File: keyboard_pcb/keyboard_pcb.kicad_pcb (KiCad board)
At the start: 2 copper layers, 190 parts, among them SW1 ESC, SW10 F9, SW11 F10, SW12 F11, SW13 F12, SW14 PRNTSC, SW15 SCRLLK, SW16 PBRK, SW17 `, SW18 #1, SW19 #2, SW2 F1, SW20 #3, SW21 #4, SW22 #5, SW23 #6, SW24 #7, SW25 #8, SW26 #9, SW27 #0, SW28 -, SW29 =, SW3 F2, SW30 BKSPC, SW31 INS, SW32 HOME, SW33 PGUP, SW34 TAB, SW35 Q, SW36 W, SW37 E, SW38 R, SW39 T, SW4 F3, SW40 Y, SW41 U, SW42 I, SW43 O, SW44 P, SW45 [, SW46 ], SW47 \, SW48 DEL, SW49 END, SW5 F4, SW50 PGDN, SW51 CAPSLK, SW52 A, SW53 S, SW54 D, SW55 F, SW56 G, SW57 H, SW58 J, SW59 K, SW6 F5, SW60 L, SW61 ;, SW62 ', SW63 ENTER, SW64 LSHIFT, SW65 Z, SW66 X, SW67 C, SW68 V, SW69 B, SW7 F6, SW70 N, SW71 M, SW72 ,, SW73 ., SW74 /, SW75 RSHIFT, SW76 UP, SW77 LCTRL, SW78 LWIN, SW79 LALT, SW8 F7, SW80 SPACE, SW81 RALT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

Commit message: Finalize key switch positions
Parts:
- D1, D10, D11, D12, D13, D14, D15, D16, D17, D18, D19, D2, D20, D21, D22, D23, D24, D25, D26, D27, D28, D29, D3, D30, D31, D32, D33, D34, D35, D36, D37, D38, D39, D4, D40, D41, D42, D43, D44, D45, D46, D47, D48, D49, D5, D50, D51, D52, D53, D54, D55, D56, D57, D58, D59, D6, D60, D61, D62, D63, D64, D65, D66, D67, D68, D69, D7, D70, D71, D72, D73, D74, D75, D76, D77, D78, D79, D8, D80, D81, D82, D83, D84, D85, D86, D87, D9: moved to B.Cu
- moved D14 56.1 mm to (379.4, 151.6)
- moved D15 56.1 mm to (398.5, 151.6)
- moved D16 56.1 mm to (417.5, 151.6)
- moved SW14 55.9 mm to (382.0, 141.8)
- moved SW15 55.9 mm to (401.0, 141.8)
- moved SW16 55.9 mm to (420.1, 141.8)
- moved D31 55.6 mm to (379.4, 173.0)
- moved D32 55.6 mm to (398.5, 173.0)
- moved D33 55.6 mm to (417.5, 173.0)
- moved D48 55.6 mm to (379.4, 192.1)
- moved D49 55.6 mm to (398.5, 192.1)
- moved D50 55.6 mm to (417.5, 192.1)
- moved D76 55.6 mm to (398.5, 230.2)
- moved D85 55.6 mm to (379.4, 249.2)
- moved D86 55.6 mm to (398.5, 249.2)
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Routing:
- net Net-(D50-A): track 0.00 -> 8.20 mm
- net Net-(D49-A): track 0.00 -> 8.20 mm
- net Net-(D47-A): track 0.00 -> 8.20 mm
- net Net-(D46-A): track 0.00 -> 8.20 mm
- net Net-(D43-A): track 0.00 -> 8.20 mm
- net Net-(D42-A): track 0.00 -> 8.20 mm
- net Net-(D37-A): track 0.00 -> 8.20 mm
- net Net-(D87-A): track 0.00 -> 8.20 mm
- net Net-(D86-A): track 0.00 -> 8.20 mm
- net Net-(D84-A): track 0.00 -> 8.20 mm
- net Net-(D83-A): track 0.00 -> 8.20 mm
- net Net-(D82-A): track 0.00 -> 8.20 mm
- net Net-(D81-A): track 0.00 -> 8.20 mm
- net Net-(D70-A): track 0.00 -> 8.20 mm
- net Net-(D76-A): track 0.00 -> 8.20 mm
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
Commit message: Add row/column traces
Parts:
- C1, C2, C3, C4, C5, C6, C7, F1, R1, R2, R3, R4, SW88, U1, USB1, Y1: moved to B.Cu
- moved R1 173.3 mm to (228.6, 237.3), turned to 180 degrees
- moved F1 78.4 mm to (280.2, 149.2), turned to 90 degrees
- moved C7 45.4 mm to (223.0, 238.9)
- moved C3 39.8 mm to (258.0, 265.1)
- moved C4 39.2 mm to (258.0, 268.3)
- moved C6 37.6 mm to (223.0, 248.4), turned to 180 degrees
- moved R2 36.5 mm to (284.2, 154.0), turned to -90 degrees
- moved R4 33.0 mm to (249.2, 250.0), turned to 180 degrees
- moved C5 31.6 mm to (258.0, 271.5)
- moved C2 30.7 mm to (258.0, 261.9)
- moved R3 30.3 mm to (281.0, 154.0), turned to -90 degrees
- moved Y1 30.0 mm to (223.0, 243.7), turned to 90 degrees
- moved C1 24.3 mm to (251.4, 245.3), turned to 180 degrees
- turned SW88 to 180 degrees
- turned U1 to 180 degrees
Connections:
- U1 pad 10: COL11 -> COL10
- U1 pad 11: COL12 -> COL11
- U1 pad 18: COL13 -> COL12
- U1 pad 19: COL14 -> COL13
- U1 pad 20: COL15 -> COL14
- U1 pad 21: COL16 -> COL15
- U1 pad 22: unconnected-(U1-PD5-Pad22) -> COL16
- U1 pad 29: COL5 -> COL4
- U1 pad 30: COL6 -> COL5
- U1 pad 31: COL7 -> COL6
- U1 pad 32: COL8 -> COL7
- U1 pad 8: COL9 -> COL8
- U1 pad 9: COL10 -> COL9
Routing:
- net ROW1: track 0.00 -> 373.5 mm, vias 0 -> 17
- net ROW0: track 0.00 -> 367.1 mm, vias 0 -> 16
- net ROW2: track 0.00 -> 364.8 mm, vias 0 -> 17
- net ROW5: track 0.00 -> 356.7 mm, vias 0 -> 11
- net ROW4: track 0.00 -> 334.9 mm, vias 0 -> 13
- net ROW3: track 0.00 -> 280.9 mm, vias 0 -> 13
- net COL10: track 0.00 -> 130.2 mm
- net COL11: track 0.00 -> 129.7 mm
- net COL13: track 0.00 -> 122.6 mm
- net COL12: track 0.00 -> 122.0 mm
- net COL6: track 0.00 -> 117.0 mm
- net COL2: track 0.00 -> 117.0 mm
- net COL0: track 0.00 -> 112.1 mm
- net COL15: track 0.00 -> 99.7 mm
- net COL16: track 0.00 -> 99.2 mm
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
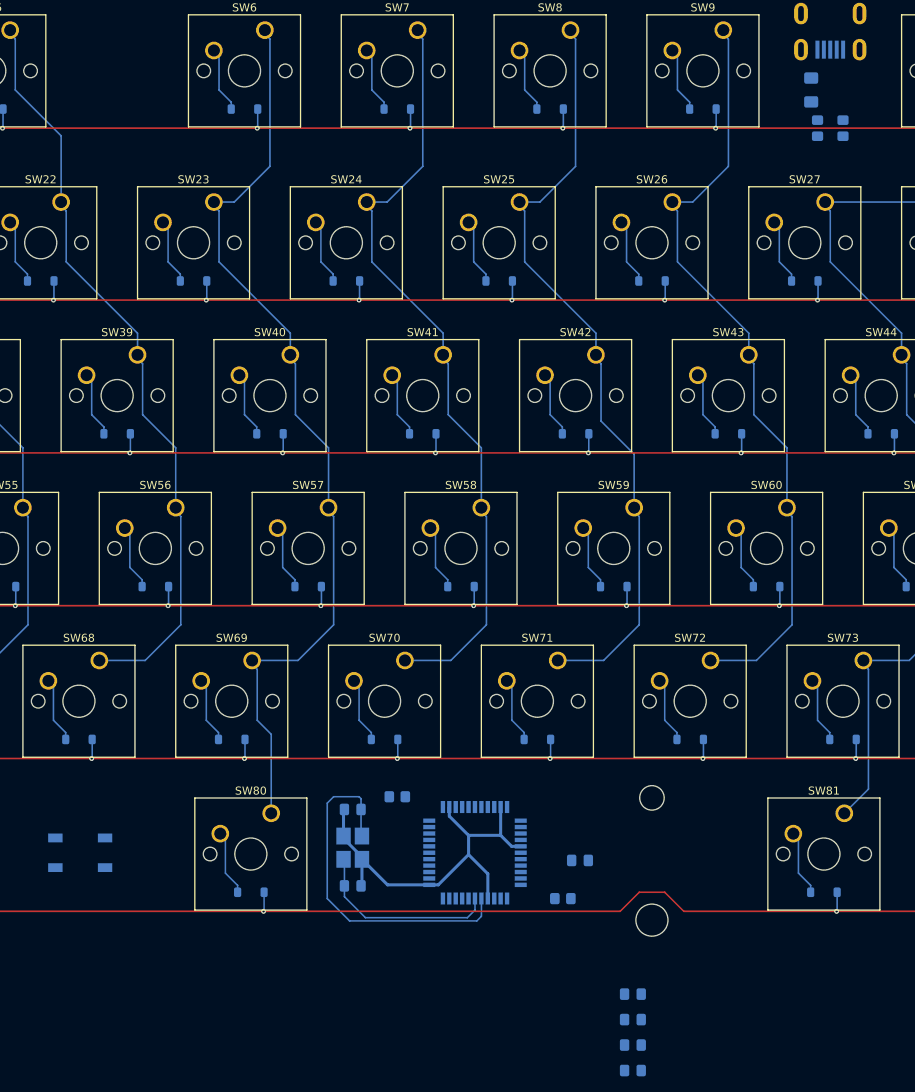
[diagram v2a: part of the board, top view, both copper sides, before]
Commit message: MCU routing except row/column
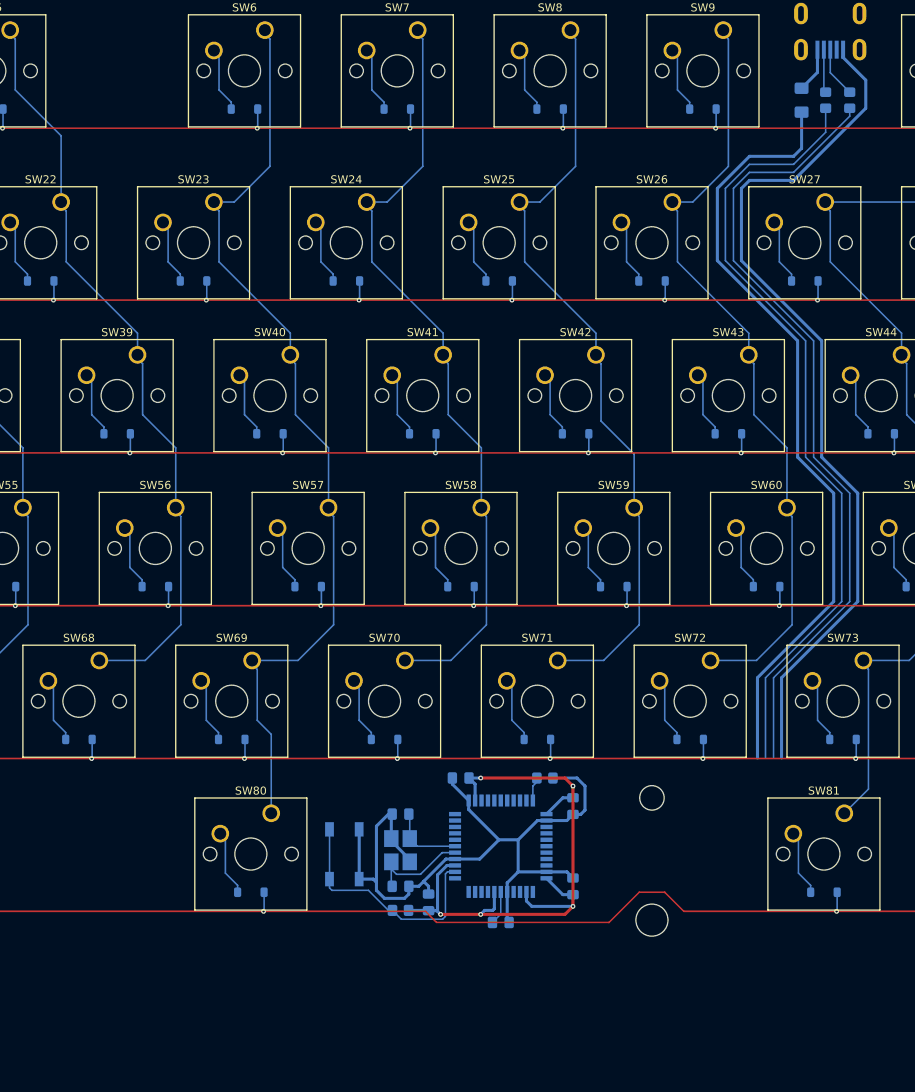
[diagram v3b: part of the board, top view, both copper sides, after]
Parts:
- moved C2 34.4 mm to (236.5, 235.0), turned to 180 degrees
- moved SW88 32.9 mm to (222.0, 244.5), turned to 90 degrees
- moved C4 31.1 mm to (232.5, 250.5), turned to 90 degrees
- moved C3 27.6 mm to (250.5, 238.5), turned to -90 degrees
- moved C5 24.1 mm to (250.5, 248.5), turned to 90 degrees
- moved R4 20.3 mm to (229.0, 251.5)
- moved R1 18.5 mm to (247.0, 235.0), turned to 0 degrees
- moved C1 12.5 mm to (241.5, 253.0), turned to 0 degrees
- moved C7 11.3 mm to (229.0, 248.5), turned to 180 degrees
- moved C6 10.7 mm to (229.0, 239.5), turned to 0 degrees
- moved Y1 5.96 mm to (229.0, 244.0), turned to -90 degrees
- moved R3 3.63 mm to (282.0, 150.5)
- moved R2 3.59 mm to (285.0, 150.5)
- moved U1 3.32 mm to (241.5, 243.5), turned to 90 degrees
- moved F1 1.75 mm to (279.0, 150.5)
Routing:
- net +5V: track 0.00 -> 180.3 mm, vias 0 -> 5
- net GND: track 50.9 -> 204.8 mm
- net Net-(U1-D+): track 0.00 -> 100.2 mm
- net Net-(U1-D-): track 0.00 -> 99.3 mm
- net Net-(U1-XTAL2): track 44.1 -> 13.3 mm
- net Net-(U1-~{RESET}): track 0.00 -> 30.1 mm
- net Net-(U1-XTAL1): track 23.9 -> 9.14 mm
- net D+: track 0.00 -> 6.30 mm
- net VCC: track 0.00 -> 5.63 mm
- net D-: track 0.00 -> 5.39 mm
- net Net-(U1-UCAP): track 0.00 -> 4.23 mm
- net Net-(U1-~{HWB}/PE2): track 0.00 -> 3.01 mm
- net ROW5: track 356.7 -> 357.8 mm

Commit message: PCB complete routing
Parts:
- moved USB1 65.9 mm to (239.7, 89.7)
- moved D36 65.3 mm to (93.7, 142.9)
- moved D38 65.3 mm to (131.8, 142.9)
- moved D39 65.3 mm to (150.8, 142.9)
- moved D41 65.3 mm to (188.9, 142.9)
- moved D43 65.3 mm to (227.0, 142.9)
- moved D44 65.3 mm to (246.1, 142.9)
- moved D45 65.3 mm to (265.1, 142.9)
- moved D48 65.3 mm to (336.6, 142.9)
- moved D50 65.3 mm to (374.6, 142.9)
- moved D64 65.3 mm to (57.9, 181.0)
- moved D67 65.3 mm to (127.0, 181.0)
- moved D69 65.3 mm to (165.1, 181.0)
- moved D71 65.3 mm to (203.2, 181.0)
- moved D72 65.3 mm to (222.2, 181.0)
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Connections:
- U1 pad 10: COL10 -> COL2
- U1 pad 11: COL11 -> COL3
- U1 pad 18: COL12 -> COL4
- U1 pad 19: COL13 -> COL5
- U1 pad 20: COL14 -> COL6
- U1 pad 21: COL15 -> COL7
- U1 pad 22: COL16 -> ROW4
- U1 pad 25: COL0 -> ROW3
- U1 pad 26: COL1 -> ROW2
- U1 pad 27: COL2 -> ROW1
- U1 pad 28: COL3 -> ROW0
- U1 pad 29: COL4 -> COL8
- U1 pad 30: COL5 -> COL9
- U1 pad 31: COL6 -> COL10
- U1 pad 32: COL7 -> COL11
- U1 pad 36: ROW0 -> COL12
- U1 pad 37: ROW1 -> COL13
- U1 pad 38: ROW2 -> COL14
- U1 pad 39: ROW3 -> COL15
- U1 pad 40: ROW4 -> COL16
- U1 pad 8: COL8 -> COL0
- U1 pad 9: COL9 -> COL1
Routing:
- net COL16: track 99.2 -> 287.8 mm
- net COL15: track 99.7 -> 269.3 mm
- net COL0: track 112.1 -> 276.8 mm
- net COL14: track 99.2 -> 249.1 mm
- net COL1: track 85.6 -> 224.9 mm
- net COL13: track 122.6 -> 246.6 mm
- net COL3: track 94.9 -> 210.2 mm
- net COL2: track 117.0 -> 231.3 mm
- net ROW0: track 367.1 -> 468.7 mm, vias 16 -> 17
- net COL4: track 94.9 -> 184.5 mm
- net COL12: track 122.0 -> 207.4 mm
- net ROW1: track 373.5 -> 454.2 mm, vias 17 -> 18
- net COL5: track 94.9 -> 165.3 mm
- net COL11: track 129.7 -> 197.9 mm
- net ROW2: track 364.8 -> 418.3 mm, vias 17 -> 18
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
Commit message: PCB cleanup
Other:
- board outline added: 347.7 x 119.1 mm
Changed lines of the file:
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@@
 		(tags "capacitor handsolder")
 		(property "Reference" "C5"
-			(at 0 1.68 90)
+			(at 3 0 90)
 			(layer "B.SilkS")
 			(effects
@@
 		(tags "capacitor handsolder")
 		(property "Reference" "C4"
-			(at 0 1.68 90)
+			(at 3 0 90)
 			(layer "B.SilkS")
 			(effects
@@
 		(tags "resistor handsolder")
 		(property "Reference" "R1"
-			(at 0 1.65 0)
+			(at 0 -2 0)
 			(layer "B.SilkS")
 			(effects
@@
 		(tags "capacitor handsolder")
 		(property "Reference" "C3"
-			(at 0 1.68 90)
+			(at 3 0 90)
 			(layer "B.SilkS")
 			(effects
@@
 		(tags "capacitor handsolder")
 		(property "Reference" "C6"
-			(at 0 1.68 0)
+			(at -3 0 0)
 			(layer "B.SilkS")
 			(effects
@@
 		(tags "resistor handsolder")
 		(property "Reference" "R2"
-			(at 0 1.65 90)
+			(at 3.2125 0.1375 90)
 			(layer "B.SilkS")
 			(effects
@@
 		(tags "resistor handsolder")
 		(property "Reference" "R3"
-			(at 0 1.65 90)
+			(at 3.2125 0.1375 90)
 			(layer "B.SilkS")
 			(effects
@@
 		(tags "SPST Button Switch")
 		(property "Reference" "SW88"
-			(at 0 3.6 90)
+			(at 0 -3.5 90)
 			(layer "B.SilkS")
 			(effects
@@
 		(tags "resistor handsolder")
 		(property "Reference" "R4"
-			(at 0 1.65 0)
+			(at 3 0 0)
 			(layer "B.SilkS")
 			(effects
@@
 		(tags "fuse handsolder")
 		(property "Reference" "F1"
-			(at 0 1.82 90)
+			(at -3.7125 -0.1375 90)
 			(layer "B.SilkS")
 			(effects
@@
 		(tags "capacitor handsolder")
 		(property "Reference" "C7"
-			(at 0 1.68 0)
+			(at 3 0 0)
 			(layer "B.SilkS")
 			(effects
@@
 		)
 	)
+	(gr_arc
+		(start 38.89375 207.16875)
+		(mid 37.209952 206.471298)
+		(end 36.5125 204.7875)
+		(stroke
+			(width 0.05)
+			(type default)
+		)
+		(layer "Edge.Cuts")
+	)
+	(gr_arc
+		(start 36.5125 90.4875)
+		(mid 37.209952 88.803702)
+		(end 38.89375 88.10625)
+		(stroke
+			(width 0.05)
+			(type default)
+		)
+		(layer "Edge.Cuts")
+	)
+	(gr_arc
+		(start 381.79375 88.10625)
+		(mid 383.477548 88.803702)
+		(end 384.175 90.4875)
+		(stroke
+			(width 0.05)
+			(type default)
+		)
+		(layer "Edge.Cuts")
+	)
+	(gr_line
+		(start 384.175 90.4875)
+		(end 384.175 204.7875)
+		(stroke
+			(width 0.05)
+			(type default)
+		)
+		(layer "Edge.Cuts")
+	)
+	(gr_line
+		(start 36.5125 204.7875)
+		(end 36.5125 90.4875)
+		(stroke
+			(width 0.05)
+			(type default)
+		)
+		(layer "Edge.Cuts")
+	)
+	(gr_line
+		(start 38.89375 88.10625)
+		(end 381.79375 88.10625)
+		(stroke
+			(width 0.05)
+			(type default)
+		)
+		(layer "Edge.Cuts")
+	)
+	(gr_arc
+		(start 384.175 204.7875)
+		(mid 383.477548 206.471298)
+		(end 381.79375 207.16875)
+		(stroke
+			(width 0.05)
+			(type default)
+		)
+		(layer "Edge.Cuts")
+	)
+	(gr_line
+		(start 381.79375 207.16875)
+		(end 38.89375 207.16875)
+		(stroke
+			(width 0.05)
+			(type default)
+		)
+		(layer "Edge.Cuts")
+	)
 	(segment
 		(start 200.4625 202.5)
@@
 	)
 	(segment
-		(start 231.5 185.5)
-		(end 212.259358 185.5)
+		(start 214 188.5)
+		(end 212.065686 188.5)
 		(width 0.2)
 		(layer "F.Cu")
@@
 	)
 	(segment
-		(start 211.629679 186.129679)
-		(end 211.629679 202.370321)
+		(start 221 188.5)
+		(end 218.5 191)
+		(width 0.2)
+		(layer "F.Cu")
+		(net 102)
+	)
+	(segment
+		(start 228.5 188.5)
+		(end 221 188.5)
 		(width 0.2)
 		(layer "F.Cu")
@@
 	(segment
 		(start 232.5 184.5)
-		(end 231.5 185.5)
+		(end 228.5 188.5)
 		(width 0.2)
 		(layer "F.Cu")
@@
 	)
 	(segment
-		(start 212.259358 185.5)
-		(end 211.629679 186.129679)
+		(start 216.5 191)
+		(end 214 188.5)
 		(width 0.2)
 		(layer "F.Cu")
@@
 	)
 	(segment
-		(start 211.629679 202.370321)
+		(start 211.6 188.965686)
+		(end 211.6 202.4)
+		(width 0.2)
+		(layer "F.Cu")
+		(net 102)
+	)
+	(segment
+		(start 211.6 202.4)
 		(end 211 203)
 		(width 0.2)
@@
 		(net 102)
 	)
+	(segment
+		(start 218.5 191)
+		(end 216.5 191)
+		(width 0.2)
+		(layer "F.Cu")
+		(net 102)
+	)
+	(segment
+		(start 212.065686 188.5)
+		(end 211.6 188.965686)
+		(width 0.2)
+		(layer "F.Cu")
+		(net 102)
+	)
 	(via
 		(at 211 203)
@@
 	)
 	(segment
-		(start 211 186.193672)
-		(end 211 202)
+		(start 212 188)
+		(end 211 189)
+		(width 0.2)
+		(layer "F.Cu")
+		(net 104)
+	)
+	(segment
+		(start 221 188)
+		(end 218.5 185.5)
 		(width 0.2)
 		(layer "F.Cu")
@@
 	)
 	(segment
-		(start 212.096836 185.096836)
-		(end 211 186.193672)
+		(start 216.5 185.5)
+		(end 214 188)
 		(width 0.2)
 		(layer "F.Cu")
@@
 	)
 	(segment
-		(start 212.1 185.1)
-		(end 212.096836 185.096836)
+		(start 214 188)
+		(end 212 188)
 		(width 0.2)
 		(layer "F.Cu")
@@
 	)
 	(segment
-		(start 230.4 185.1)
-		(end 212.1 185.1)
+		(start 211 189)
+		(end 211 202)
 		(width 0.2)
 		(layer "F.Cu")
@@
 	(segment
 		(start 231 184.5)
-		(end 230.4 185.1)
+		(end 227.5 188)
+		(width 0.2)
+		(layer "F.Cu")
+		(net 104)
+	)
+	(segment
+		(start 218.5 185.5)
+		(end 216.5 185.5)
+		(width 0.2)
+		(layer "F.Cu")
+		(net 104)
+	)
+	(segment
+		(start 227.5 188)
+		(end 221 188)
 		(width 0.2)
 		(layer "F.Cu")
